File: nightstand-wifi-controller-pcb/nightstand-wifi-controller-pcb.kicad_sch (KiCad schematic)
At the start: 8 parts, among them J2 Conn_01x06_Socket, J4 Screw_Terminal_01x02, J5 Screw_Terminal_01x02, K2 FINDER-36.11, Q2 PN2222A

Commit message: First Approach to a PCB design
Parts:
- J2: footprint (none) -> Connector_PinSocket_1.27mm:PinSocket_1x06_P1.27mm_Vertical
- J4, J5: footprint (none) -> TerminalBlock:TerminalBlock_Altech_AK300-2_P5.00mm
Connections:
- no-connect marks 2 -> 27
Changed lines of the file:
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@@
   (junction (at 105.41 80.01) (diameter 0) (color 0 0 0 0)
   )
+  (junction (at 80.645 88.9) (diameter 0) (color 0 0 0 0)
+  )
+  (junction (at 80.645 83.82) (diameter 0) (color 0 0 0 0)
+  )
   (junction (at 82.55 83.82) (diameter 0) (color 0 0 0 0)
   )
+  (no_connect (at 128.27 72.39))
+  (no_connect (at 128.27 49.53))
+  (no_connect (at 158.75 46.99))
+  (no_connect (at 158.75 72.39))
+  (no_connect (at 158.75 49.53))
+  (no_connect (at 128.27 64.77))
+  (no_connect (at 128.27 77.47))
   (no_connect (at 97.79 72.39))
+  (no_connect (at 128.27 52.07))
+  (no_connect (at 158.75 77.47))
+  (no_connect (at 128.27 59.69))
+  (no_connect (at 158.75 41.91))
+  (no_connect (at 158.75 74.93))
+  (no_connect (at 158.75 57.15))
+  (no_connect (at 128.27 62.23))
+  (no_connect (at 128.27 41.91))
+  (no_connect (at 158.75 44.45))
+  (no_connect (at 158.75 59.69))
+  (no_connect (at 128.27 69.85))
+  (no_connect (at 128.27 74.93))
+  (no_connect (at 128.27 57.15))
+  (no_connect (at 158.75 52.07))
+  (no_connect (at 128.27 46.99))
+  (no_connect (at 158.75 54.61))
+  (no_connect (at 144.145 114.3))
   (no_connect (at 185.42 68.58))
+  (no_connect (at 128.27 54.61))
   (wire (pts (xy 170.18 58.42) (xy 185.42 58.42))
     (stroke (width 0) (type default))
   )
-  (wire (pts (xy 82.55 83.82) (xy 78.74 83.82))
+  (wire (pts (xy 82.55 83.82) (xy 80.645 83.82))
     (stroke (width 0) (type default))
   )
@@
     (stroke (width 0) (type default))
   )
+  (wire (pts (xy 80.645 83.82) (xy 78.74 83.82))
+    (stroke (width 0) (type default))
+  )
   (wire (pts (xy 95.25 57.15) (xy 95.25 53.34))
     (stroke (width 0) (type default))
@@
     (stroke (width 0) (type default))
   )
+  (wire (pts (xy 80.645 88.9) (xy 76.2 88.9))
+    (stroke (width 0) (type default))
+  )
   (wire (pts (xy 82.55 83.82) (xy 82.55 76.2))
     (stroke (width 0) (type default))
@@
     (stroke (width 0) (type default))
   )
-  (wire (pts (xy 83.82 88.9) (xy 76.2 88.9))
+  (wire (pts (xy 83.82 88.9) (xy 80.645 88.9))
     (stroke (width 0) (type default))
   )
@@
       (effects (font (size 1.27 1.27)) (justify left))
     )
-    (property "Footprint" "" (at 68.58 88.9 0)
+    (property "Footprint" "TerminalBlock:TerminalBlock_Altech_AK300-2_P5.00mm" (at 68.58 88.9 0)
       (effects (font (size 1.27 1.27)) hide)
     )
@@
     )
   )
+  (symbol (lib_id "power:PWR_FLAG") (at 80.645 88.9 180) (unit 1)
+    (in_bom yes) (on_board yes) (dnp no) (fields_autoplaced)
+    (property "Reference" "#FLG02" (at 80.645 90.805 0)
+      (effects (font (size 1.27 1.27)) hide)
+    )
+    (property "Value" "PWR_FLAG" (at 80.645 93.98 0)
+      (effects (font (size 1.27 1.27)))
+    )
+    (property "Footprint" "" (at 80.645 88.9 0)
+      (effects (font (size 1.27 1.27)) hide)
+    )
+    (property "Datasheet" "~" (at 80.645 88.9 0)
+      (effects (font (size 1.27 1.27)) hide)
+    )
+    (pin "1")
+    (instances
+      (project "nightstand-wifi-controller-pcb"
+        (path "/baf5fec3-ee1f-4b5c-823d-5447393c476e"
+          (reference "#FLG02") (unit 1)
+        )
+      )
+    )
+  )
   (symbol (lib_id "power:GND") (at 105.41 34.29 180) (unit 1)
     (in_bom yes) (on_board yes) (dnp no) (fields_autoplaced)
@@
       (effects (font (size 1.27 1.27)) (justify left))
     )
-    (property "Footprint" "" (at 190.5 63.5 0)
+    (property "Footprint" "Connector_PinSocket_1.27mm:PinSocket_1x06_P1.27mm_Vertical" (at 190.5 63.5 0)
       (effects (font (size 1.27 1.27)) hide)
     )
@@
     )
   )
+  (symbol (lib_id "power:PWR_FLAG") (at 80.645 83.82 0) (unit 1)
+    (in_bom yes) (on_board yes) (dnp no) (fields_autoplaced)
+    (property "Reference" "#FLG01" (at 80.645 81.915 0)
+      (effects (font (size 1.27 1.27)) hide)
+    )
+    (property "Value" "PWR_FLAG" (at 80.645 78.74 0)
+      (effects (font (size 1.27 1.27)))
+    )
+    (property "Footprint" "" (at 80.645 83.82 0)
+      (effects (font (size 1.27 1.27)) hide)
+    )
+    (property "Datasheet" "~" (at 80.645 83.82 0)
+      (effects (font (size 1.27 1.27)) hide)
+    )
+    (pin "1")
+    (instances
+      (project "nightstand-wifi-controller-pcb"
+        (path "/baf5fec3-ee1f-4b5c-823d-5447393c476e"
+          (reference "#FLG01") (unit 1)
+        )
+      )
+    )
+  )
   (symbol (lib_id "Connector:Screw_Terminal_01x02") (at 67.31 55.88 180) (unit 1)
     (in_bom yes) (on_board yes) (dnp no) (fields_autoplaced)
@@
       (effects (font (size 1.27 1.27)) (justify left))
     )
-    (property "Footprint" "" (at 67.31 55.88 0)
-      (effects (font (size 1.27 1.27)) hide)
-    )
+    (property "Footprint" "TerminalBlock:TerminalBlock_Altech_AK300-2_P5.00mm" (at 67.31 55.88 0)
+      (effects (font (size 1.27 1.27)) hide)
+    )

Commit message: Missing schematic changes
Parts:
- Q2: footprint Package_TO_SOT_THT_AKL:TO-92_Inline_Wide_EBC -> Package_TO_SOT_THT:TO-92_HandSolder
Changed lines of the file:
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@@
       (effects (font (size 1.27 1.27)) (justify left))
     )
-    (property "Footprint" "Package_TO_SOT_THT_AKL:TO-92_Inline_Wide_EBC" (at 102.87 46.99 0)
+    (property "Footprint" "Package_TO_SOT_THT:TO-92_HandSolder" (at 102.87 46.99 0)
       (effects (font (size 1.27 1.27)) hide)
     )

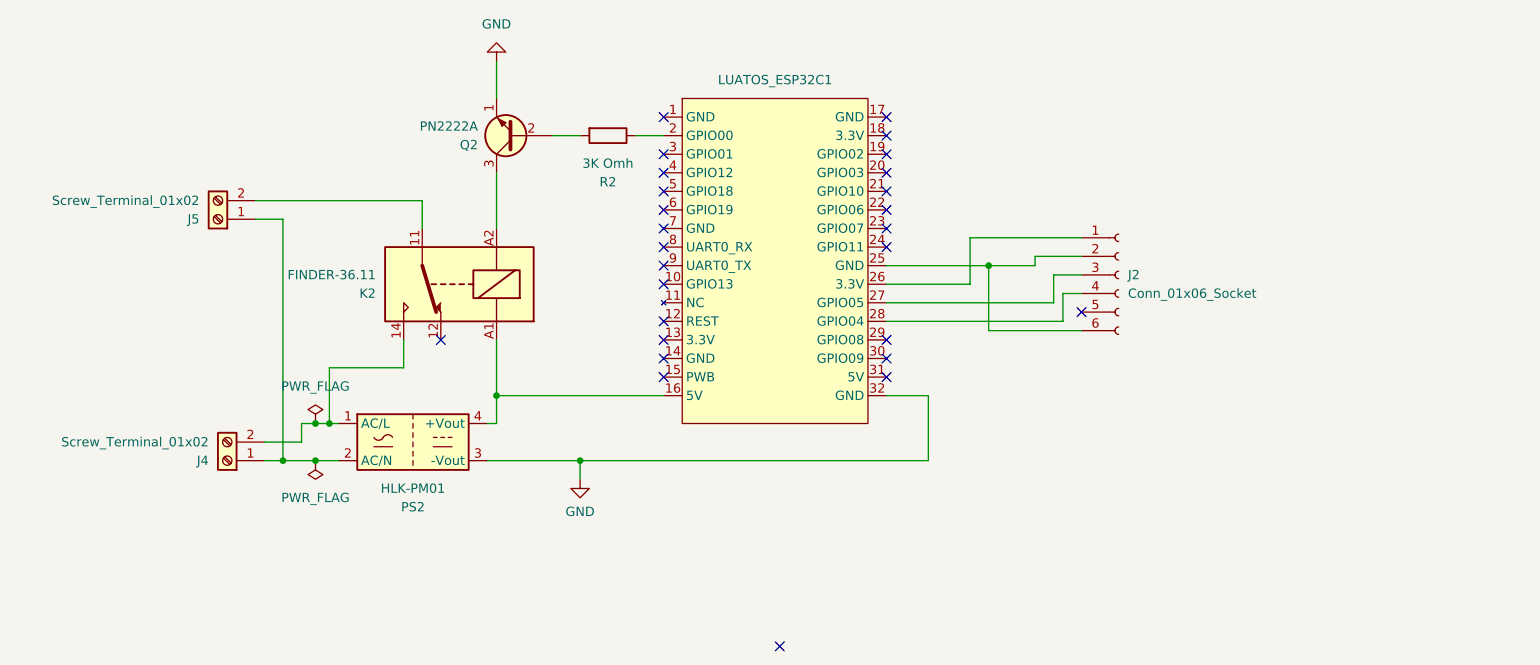
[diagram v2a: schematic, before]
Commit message: PCB design completeed and JLCPCB Design rules set up
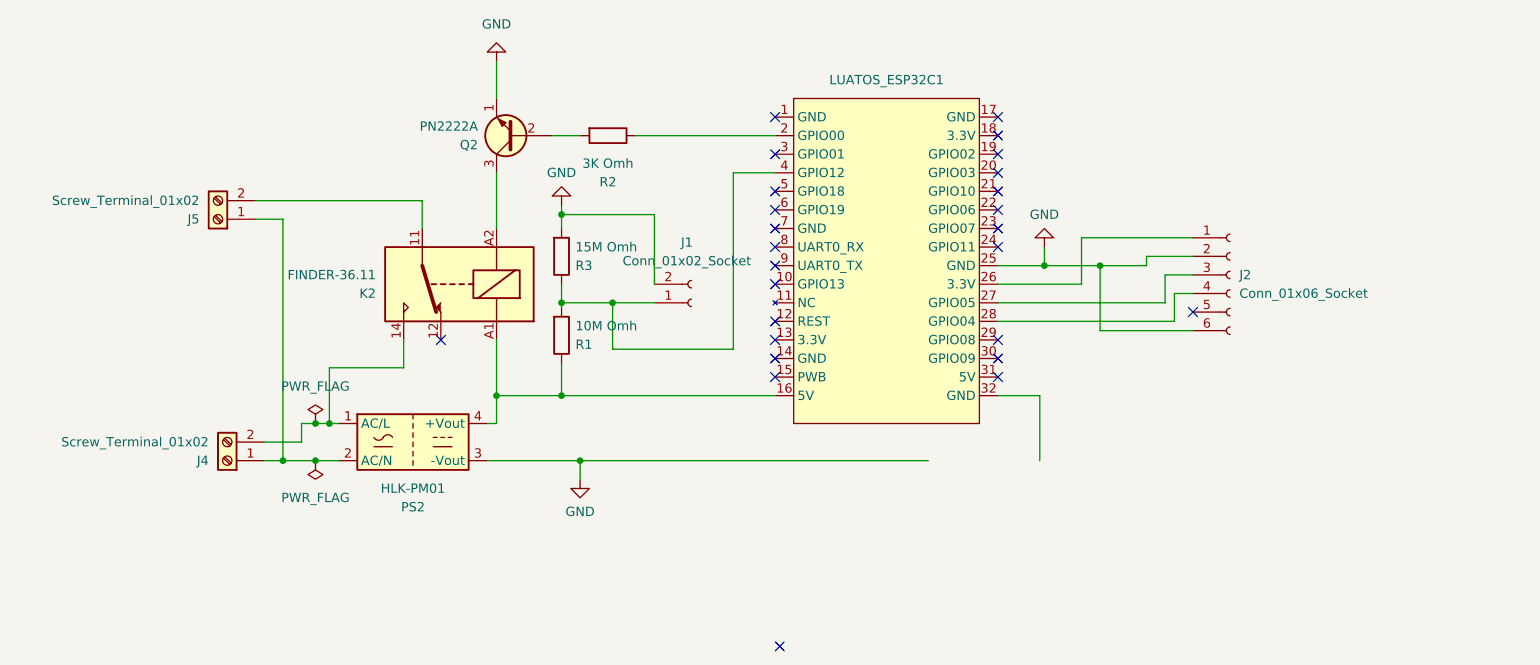
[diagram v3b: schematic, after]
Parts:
- added J1: Conn_01x02_Socket, Connector_PinSocket_1.27mm:PinSocket_1x02_P1.27mm_Vertical, symbol Connector:Conn_01x02_Socket
- added R1: 10M Omh, Resistor_THT:R_Axial_DIN0207_L6.3mm_D2.5mm_P10.16mm_Horizontal, symbol Device:R
- added R3: 15M Omh, Resistor_THT:R_Axial_DIN0207_L6.3mm_D2.5mm_P10.16mm_Horizontal, symbol Device:R
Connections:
- net GND: now also J2.2 (Pin_2), J2.6 (Pin_6), LUATOS_ESP32C1.25 (GND), J1.2 (Pin_2), R3.2; no longer LUATOS_ESP32C1.32 (GND)
- net at K2.A1, LUATOS_ESP32C1.16 (5V), PS2.4 (+Vout): now also R1.1
- net at LUATOS_ESP32C1.4 (GPIO12): now also J1.1 (Pin_1), R1.2, R3.1
- no-connect marks 27 -> 26
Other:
- moved on the sheet: J2, LUATOS_ESP32C1

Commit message: Fix on earth for mcu module
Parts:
- J1: footprint Connector_PinSocket_1.27mm:PinSocket_1x02_P1.27mm_Vertical -> Connector_PinSocket_2.54mm:PinSocket_1x02_P2.54mm_Vertical
- J2: footprint Connector_PinSocket_1.27mm:PinSocket_1x06_P1.27mm_Vertical -> Connector_PinSocket_2.54mm:PinSocket_1x06_P2.54mm_Vertical
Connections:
- net GND: now also LUATOS_ESP32C1.32 (GND)
- no-connect marks 26 -> 25
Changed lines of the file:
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@@
   (no_connect (at 143.51 46.99))
   (no_connect (at 173.99 54.61))
-  (no_connect (at 144.145 114.3))
   (no_connect (at 173.99 72.39))
   (no_connect (at 200.66 68.58))
@@
     (stroke (width 0) (type default))
   )
-  (wire (pts (xy 164.465 88.9) (xy 116.84 88.9))
+  (wire (pts (xy 116.84 88.9) (xy 179.705 88.9))
     (stroke (width 0) (type default))
   )
@@
       (effects (font (size 1.27 1.27)))
     )
-    (property "Footprint" "Connector_PinSocket_1.27mm:PinSocket_1x02_P1.27mm_Vertical" (at 132.08 67.31 0)
+    (property "Footprint" "Connector_PinSocket_2.54mm:PinSocket_1x02_P2.54mm_Vertical" (at 132.08 67.31 0)
       (effects (font (size 1.27 1.27)) hide)
     )
@@
       (effects (font (size 1.27 1.27)) (justify left))
     )
-    (property "Footprint" "Connector_PinSocket_1.27mm:PinSocket_1x06_P1.27mm_Vertical" (at 205.74 63.5 0)
-      (effects (font (size 1.27 1.27)) hide)
-    )
+    (property "Footprint" "Connector_PinSocket_2.54mm:PinSocket_1x06_P2.54mm_Vertical" (at 205.74 63.5 0)
+      (effects (font (size 1.27 1.27)) hide)
+    )

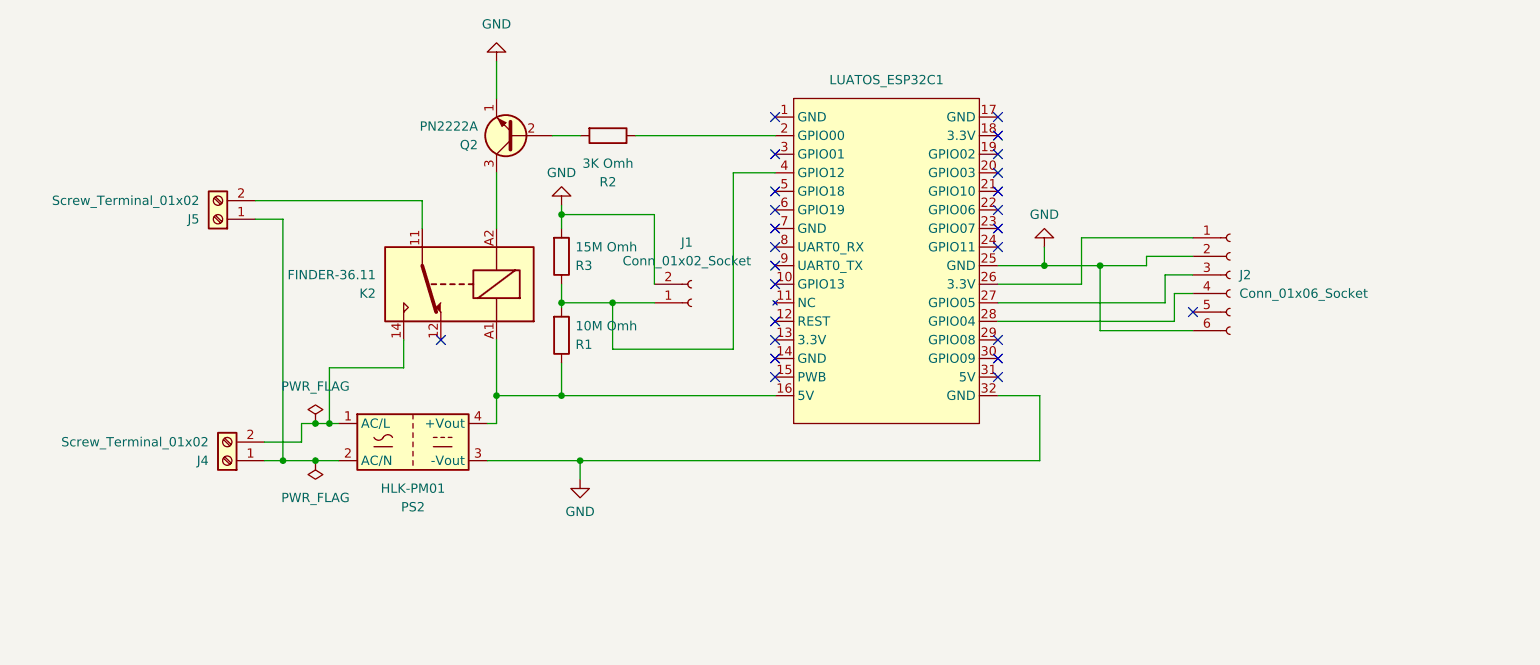
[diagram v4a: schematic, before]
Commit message: Snubber diod added to relay coil and temp sensor socket location fixed
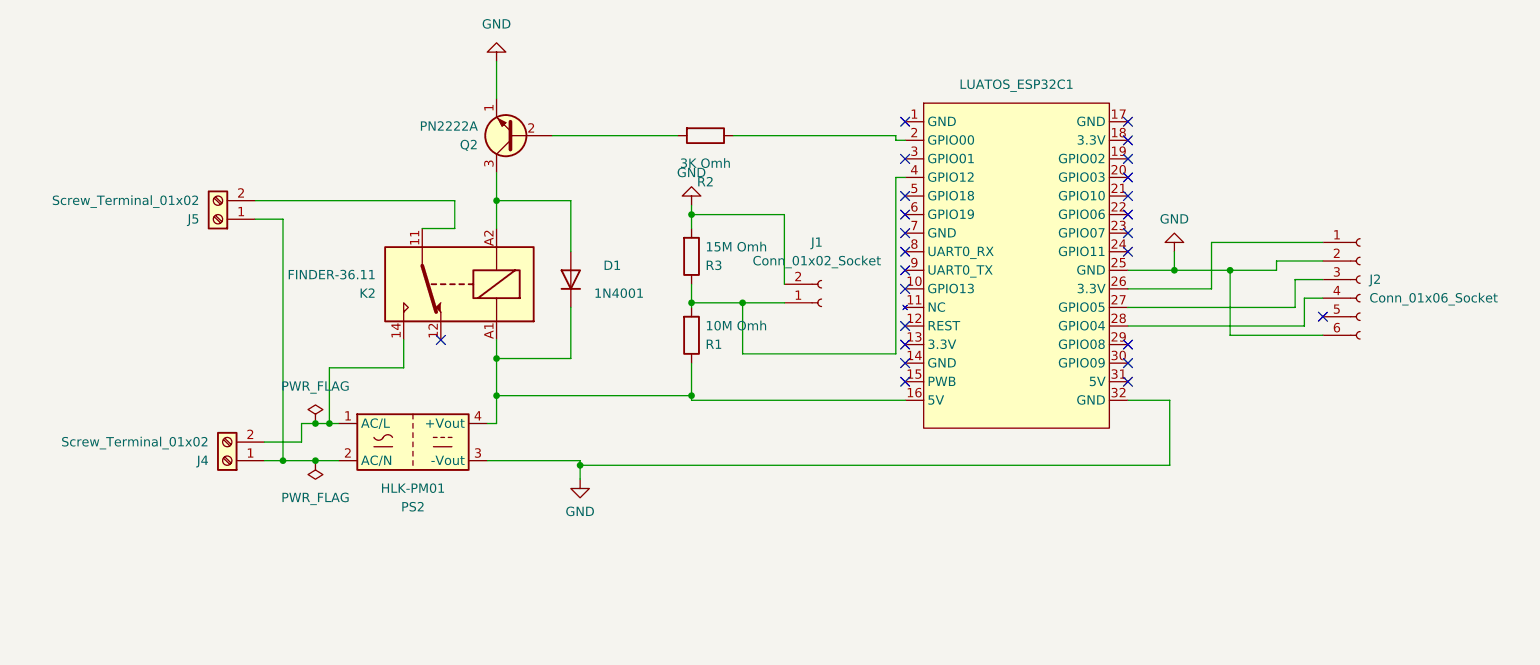
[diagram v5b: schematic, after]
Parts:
- added D1: 1N4001, Diode_THT:D_DO-41_SOD81_P10.16mm_Horizontal, symbol Diode:1N4001
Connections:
- net at K2.A1, LUATOS_ESP32C1.16 (5V), PS2.4 (+Vout)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: now also D1.1 (K)
- net at K2.A2, Q2.3 (C): now also D1.2 (A)
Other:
- moved on the sheet: J1, J2, LUATOS_ESP32C1, R1, R2, R3
